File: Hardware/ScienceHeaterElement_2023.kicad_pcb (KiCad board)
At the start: 2 copper layers, 58.9 x 46.2 mm, 16 parts, among them Q1 Si4162DY, U1 LMT85DCK

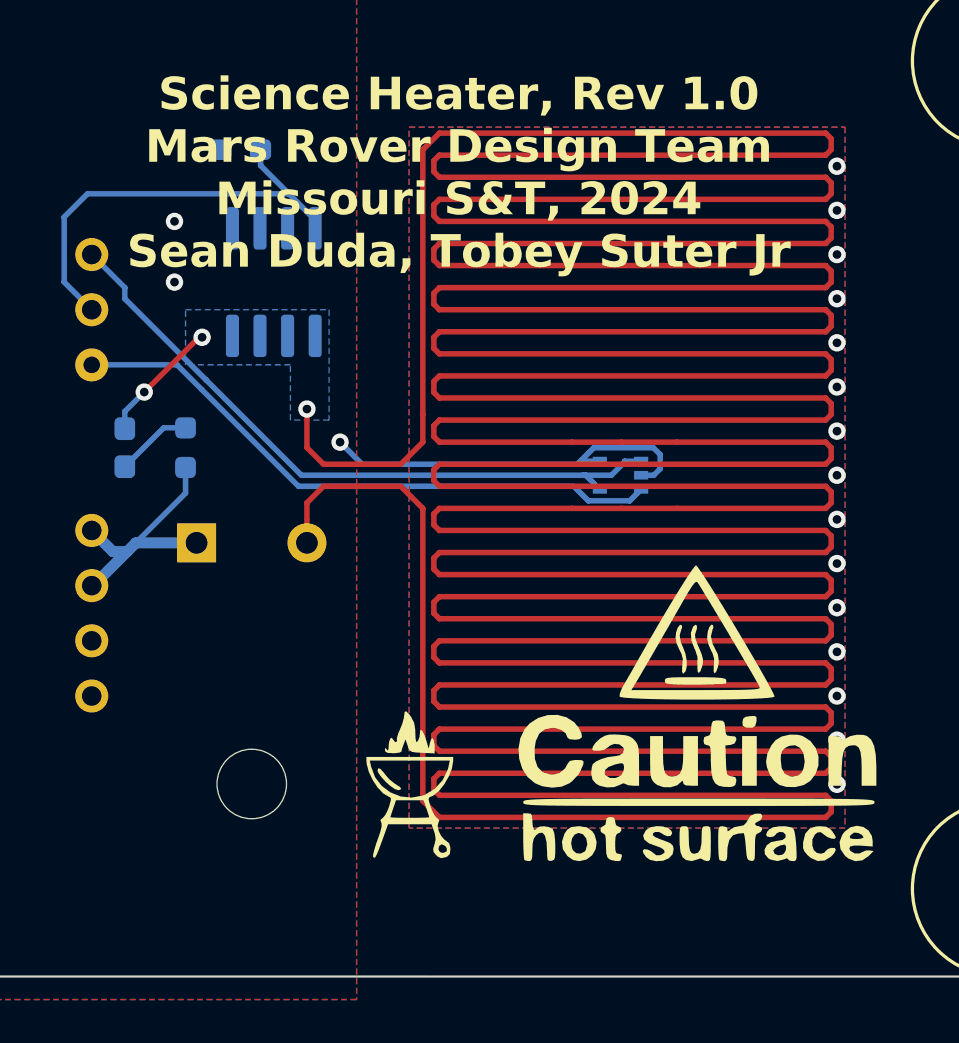
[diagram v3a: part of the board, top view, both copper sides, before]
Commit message: Replaced current limiting resistor
Replaced current limiting resistor with 2.5 Ohm resistor and changed the resistor package
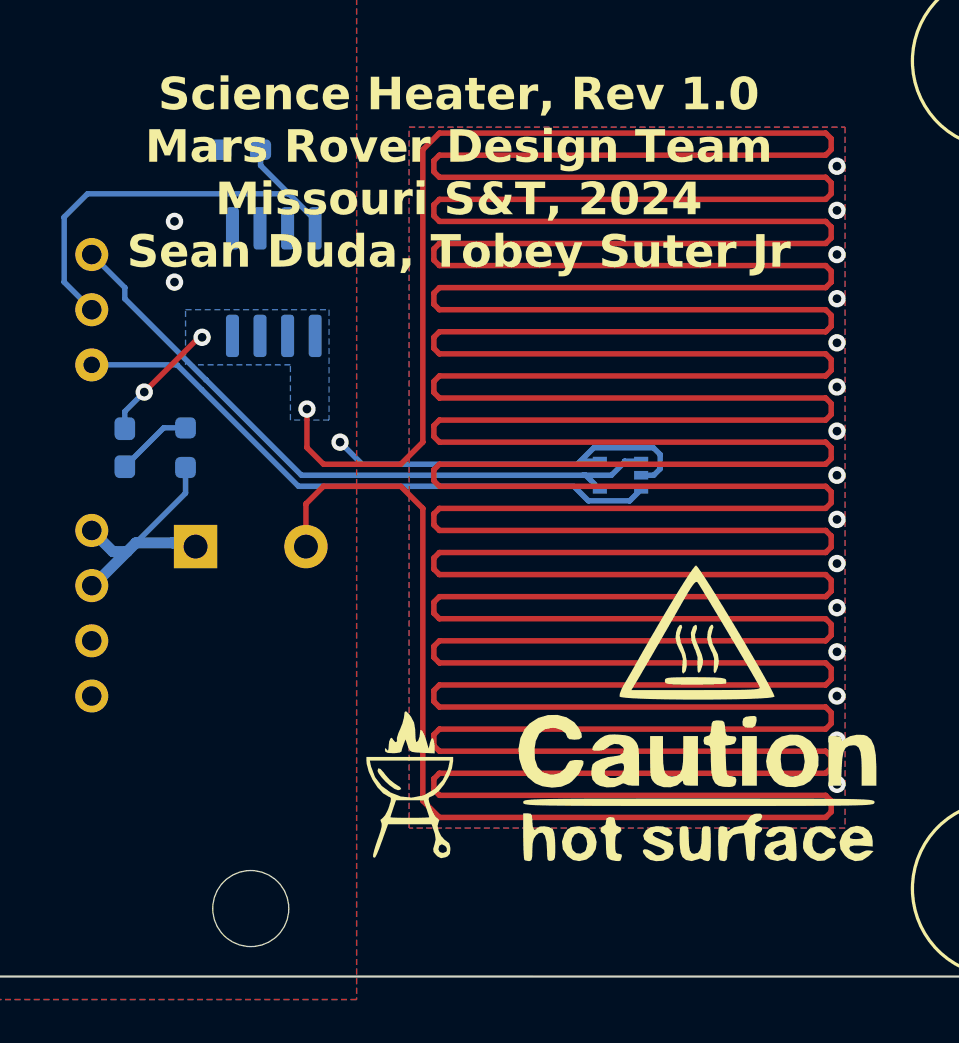
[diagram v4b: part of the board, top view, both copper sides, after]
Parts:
- R1: value 7.5 -> 2.5; footprint Package_TO_SOT_THT:TO-126-2_Horizontal_TabDown -> Package_TO_SOT_THT:TO-220-2_Horizontal_TabDown
- moved R1 0.18 mm to (140.8, 52.8)
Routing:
- net +12V: track 12.1 -> 13.2 mm

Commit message: Moved silkscreen labels
Moved silkscreen labels to where they can be seen properly
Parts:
- moved G*** 21.5 mm to (171.0, 42.0)
- moved G*** 21.5 mm to (157.8, 38.9)
- moved G*** 21.5 mm to (150.8, 42.0)
- moved G*** 21.5 mm to (164.0, 38.9)
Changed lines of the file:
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@@
   )
   (footprint "LOGO" (layer "F.Cu")
-    (at 150.61 63.532)
+    (at 150.80595 42.0182)
     (attr board_only exclude_from_pos_files exclude_from_bom)
     (fp_text reference "G***" (at -2.15 -7.34) (layer "F.SilkS") hide
@@
   )
   (footprint "LOGO" (layer "F.Cu")
-    (at 163.83 60.452)
+    (at 164.02595 38.9382)
     (attr board_only exclude_from_pos_files exclude_from_bom)
     (fp_text reference "G***" (at 5.51 -11.48) (layer "F.SilkS") hide
@@
   )
   (footprint "LOGO" (layer "B.Cu")
-    (at 170.82225 63.5 180)
+    (at 171.0182 41.9862 180)
     (attr board_only exclude_from_pos_files exclude_from_bom)
     (fp_text reference "G***" (at -2.15 7.34) (layer "B.SilkS") hide
@@
   )
   (footprint "LOGO" (layer "B.Cu")
-    (at 157.60225 60.42 180)
+    (at 157.7982 38.9062 180)
     (attr board_only exclude_from_pos_files exclude_from_bom)
     (fp_text reference "G***" (at 5.51 11.48) (layer "B.SilkS") hide
@@
   (gr_line (start 177.799901 72.6217) (end 127.119981 72.62)
     (stroke (width 0.1) (type default)) (layer "Edge.Cuts"))
-  (gr_text "Science Heater, Rev 1.0\nMars Rover Design Team\nMissouri S&T, 2024\nSean Duda, Tobey Suter Jr" (at 152.908 40.132) (layer "F.SilkS")
-    (effects (font (size 1.5 1.5) (thickness 0.3) bold) (justify bottom))
+  (gr_text "Science Heater, Rev 1.0\nMars Rover Design Team\nMissouri S&T, 2024\nSean Duda, Tobey Suter Jr" (at 163.83 62.8142) (layer "B.SilkS")
+    (effects (font (size 1.5 1.5) (thickness 0.3) bold) (justify bottom mirror))
   )
   (dimension (type aligned) (layer "Dwgs.User")
